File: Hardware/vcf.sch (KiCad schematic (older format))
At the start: 67 parts, among them U1 TL074, U2 TL074, U3 TL074

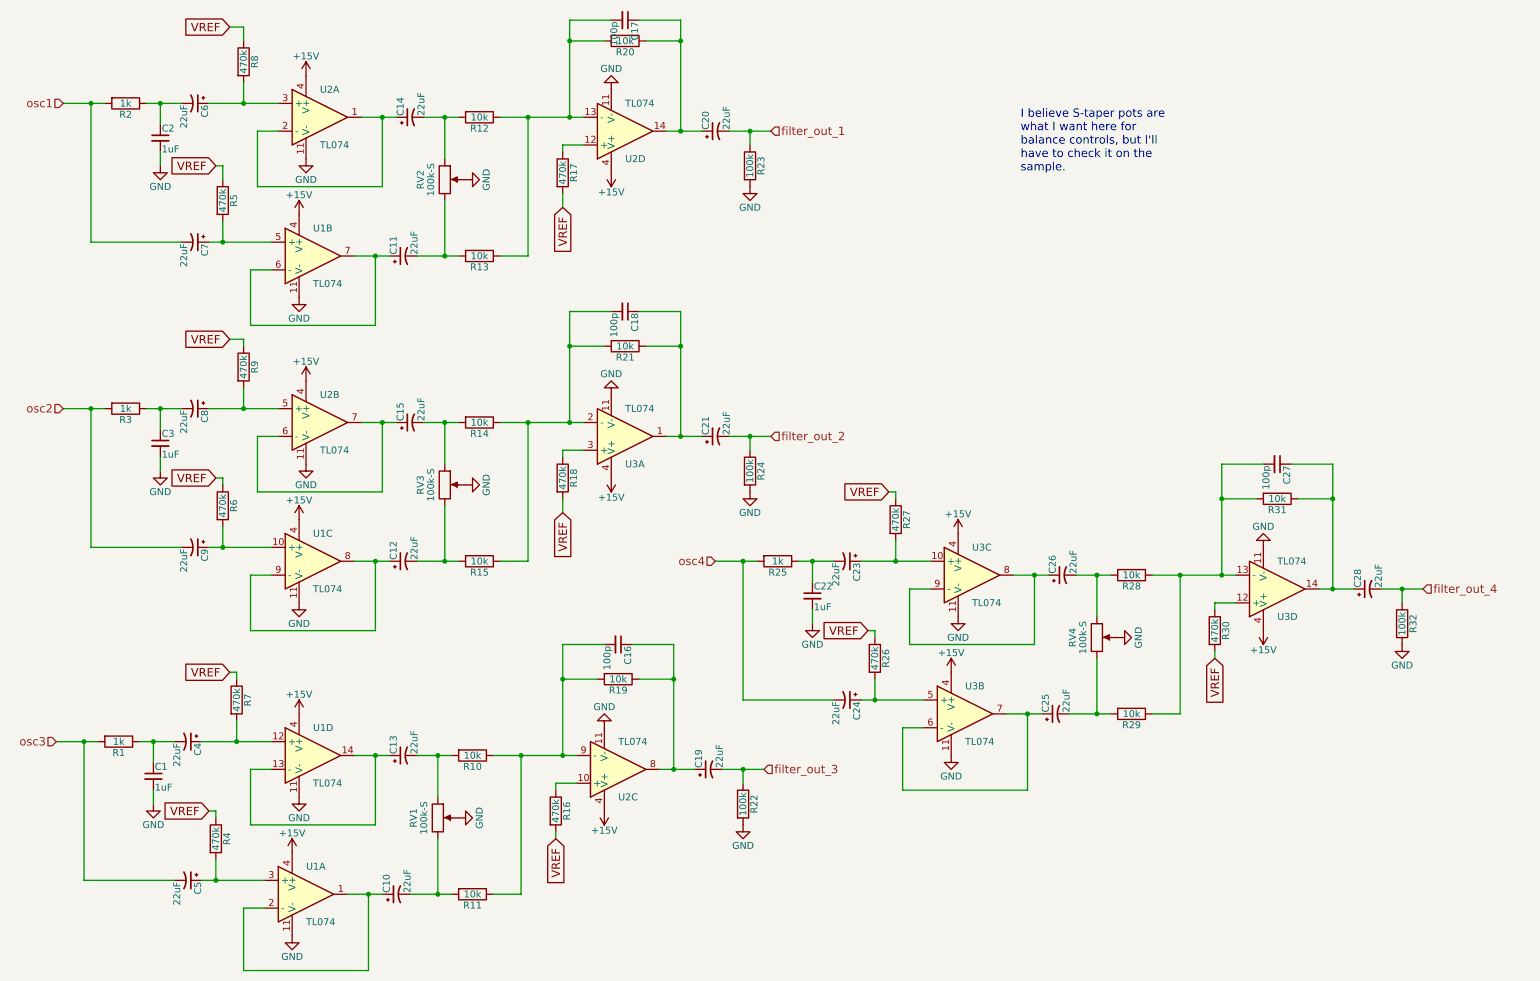
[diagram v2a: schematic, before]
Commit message: fix annotation and footprints for multi-part op amps.
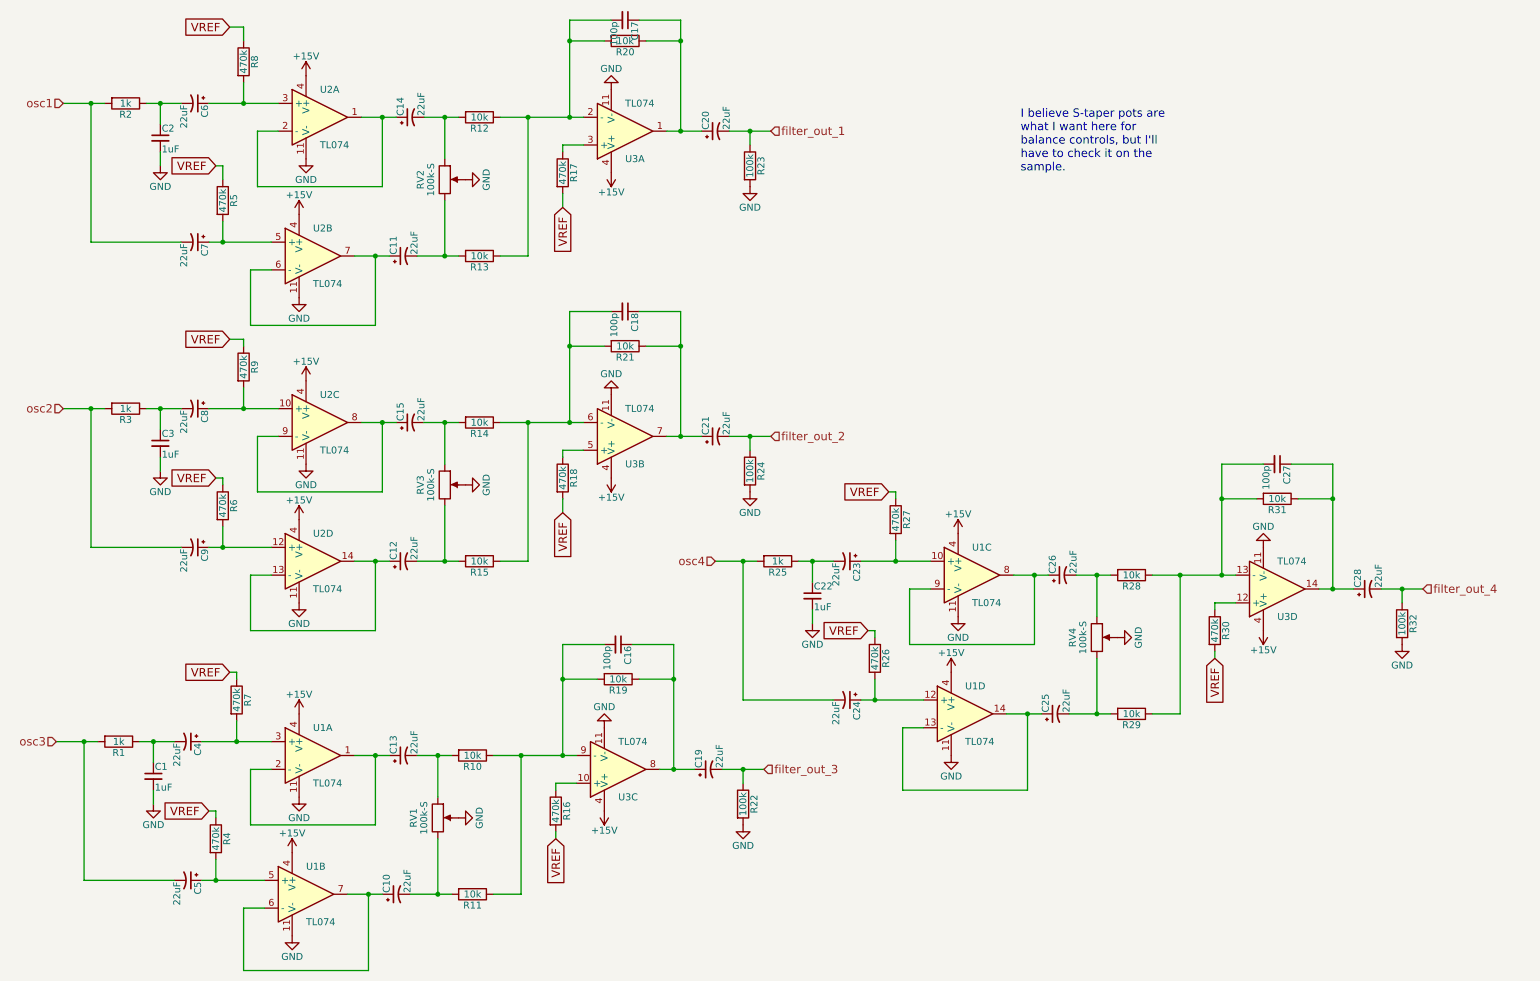
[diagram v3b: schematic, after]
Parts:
- renumbered U3 to U1, U1 to U2, U2 to U3
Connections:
- net at C17.2, R12.1, R13.1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: now also U3.2 (-); no longer U3.13 (-)
- net at R17.1: now also U3.3 (+); no longer U3.12 (+)
- net at C17.1, C20.1, R20.1: now also U3.1; no longer U3.14
- net at C8.1, R9.2: now also U2.10 (+); no longer U2.5 (+)
- net at C9.1, R6.2: now also U2.12 (+); no longer U2.10 (+)
- net at C18.2, R14.1, R15.1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: now also U3.6 (-); no longer U3.2 (-)
- net at C18.1, C21.1, R21.1: now also U3.7; no longer U3.1
- net at R18.1: now also U3.5 (+); no longer U3.3 (+)
- net at C4.1, R7.2: now also U1.3 (+); no longer U1.12 (+)
- net at C5.1, R4.2: now also U1.5 (+); no longer U1.3 (+)
- net at C24.1, R26.2: now also U1.12 (+); no longer U1.5 (+)
- new net: C15.1, U2.8, U2.9 (-)
- new net: C12.1, U2.13 (-), U2.14
- new net: C13.1, U1.1, U1.2 (-)
- new net: C10.1, U1.6 (-), U1.7
- new net: C25.1, U1.13 (-), U1.14
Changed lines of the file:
@@
 $EndComp
 $Comp
-L TL074 U1
+L TL074 U2
 U 2 1 5C37EB17
 P 2600 2200
-F 0 "U1" H 2600 2400 50  0000 L CNN
+F 0 "U2" H 2600 2400 50  0000 L CNN
 F 1 "TL074" H 2600 2000 50  0000 L CNN
 F 2 "digikey-footprints:SOIC-14_W3.9mm" H 2550 2300 50  0001 C CNN
@@
 $EndComp
 $Comp
-L TL074 U2
-U 4 1 5C37F61B
+L TL074 U3
+U 1 1 5C37F61B
 P 4850 1300
-F 0 "U2" H 4850 1500 50  0000 L CNN
+F 0 "U3" H 4850 1500 50  0000 L CNN
 F 1 "TL074" H 4850 1100 50  0000 L CNN
 F 2 "digikey-footprints:SOIC-14_W3.9mm" H 4800 1400 50  0001 C CNN
 F 3 "" H 4900 1500 50  0001 C CNN
-	4    4850 1300
+	1    4850 1300
 	1    0    0    1
 $EndComp
@@
 $Comp
 L TL074 U2
-U 2 1 5C389FC9
+U 3 1 5C389FC9
 P 2650 3400
 F 0 "U2" H 2650 3600 50  0000 L CNN
@@
 F 2 "digikey-footprints:SOIC-14_W3.9mm" H 2600 3500 50  0001 C CNN
 F 3 "" H 2700 3600 50  0001 C CNN
-	2    2650 3400
+	3    2650 3400
 	1    0    0    -1
 $EndComp
@@
 $EndComp
 $Comp
-L TL074 U1
-U 3 1 5C389FF8
+L TL074 U2
+U 4 1 5C389FF8
 P 2600 4400
-F 0 "U1" H 2600 4600 50  0000 L CNN
+F 0 "U2" H 2600 4600 50  0000 L CNN
 F 1 "TL074" H 2600 4200 50  0000 L CNN
 F 2 "digikey-footprints:SOIC-14_W3.9mm" H 2550 4500 50  0001 C CNN
 F 3 "" H 2650 4600 50  0001 C CNN
-	3    2600 4400
+	4    2600 4400
 	1    0    0    -1
 $EndComp
@@
 $Comp
 L TL074 U3
-U 1 1 5C38A035
+U 2 1 5C38A035
 P 4850 3500
 F 0 "U3" H 4850 3700 50  0000 L CNN
@@
 F 2 "digikey-footprints:SOIC-14_W3.9mm" H 4800 3600 50  0001 C CNN
 F 3 "" H 4900 3700 50  0001 C CNN
-	1    4850 3500
+	2    4850 3500
 	1    0    0    1
 $EndComp
@@
 $Comp
 L TL074 U1
-U 4 1 5C38A5BF
+U 1 1 5C38A5BF
 P 2600 5800
 F 0 "U1" H 2600 6000 50  0000 L CNN
@@
 F 2 "digikey-footprints:SOIC-14_W3.9mm" H 2550 5900 50  0001 C CNN
 F 3 "" H 2650 6000 50  0001 C CNN
-	4    2600 5800
+	1    2600 5800
 	1    0    0    -1
 $EndComp
@@
 $Comp
 L TL074 U1
-U 1 1 5C38A5EE
+U 2 1 5C38A5EE
 P 2550 6800
 F 0 "U1" H 2550 7000 50  0000 L CNN
@@
 F 2 "digikey-footprints:SOIC-14_W3.9mm" H 2500 6900 50  0001 C CNN
 F 3 "" H 2600 7000 50  0001 C CNN
-	1    2550 6800
+	2    2550 6800
 	1    0    0    -1
 $EndComp
@@
 $EndComp
 $Comp
-L TL074 U2
+L TL074 U3
 U 3 1 5C38A62B
 P 4800 5900
-F 0 "U2" H 4800 6100 50  0000 L CNN
+F 0 "U3" H 4800 6100 50  0000 L CNN
 F 1 "TL074" H 4800 5700 50  0000 L CNN
 F 2 "digikey-footprints:SOIC-14_W3.9mm" H 4750 6000 50  0001 C CNN
@@
 $EndComp
 $Comp
-L TL074 U3
+L TL074 U1
 U 3 1 5C38B2F3
 P 7350 4500
-F 0 "U3" H 7350 4700 50  0000 L CNN
+F 0 "U1" H 7350 4700 50  0000 L CNN
 F 1 "TL074" H 7350 4300 50  0000 L CNN
 F 2 "digikey-footprints:SOIC-14_W3.9mm" H 7300 4600 50  0001 C CNN
@@
 $EndComp
 $Comp
-L TL074 U3
-U 2 1 5C38B322
+L TL074 U1
+U 4 1 5C38B322
 P 7300 5500
-F 0 "U3" H 7300 5700 50  0000 L CNN
+F 0 "U1" H 7300 5700 50  0000 L CNN
 F 1 "TL074" H 7300 5300 50  0000 L CNN
 F 2 "digikey-footprints:SOIC-14_W3.9mm" H 7250 5600 50  0001 C CNN
 F 3 "" H 7350 5700 50  0001 C CNN
-	2    7300 5500
-	1    0    0    -1
-$EndComp
+	4    7300 5500
+	1    0    0    -1
+$EndComp

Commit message: complete initial PCB layout. CapSense buttons still not done, but everything else should be there. I had to increase to a 4-layer board to keep the dimensions 8"x4".
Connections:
- net +15V: now also U1.11 (V-); no longer U1.4 (V+)
- net GND: now also U1.4 (V+); no longer U1.11 (V-)
- net at C13.1, U1.1: now also U1.3 (+); no longer U1.2 (-)
- net at C4.1, R7.2: now also U1.2 (-); no longer U1.3 (+)
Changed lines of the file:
@@
 F 3 "" H 2650 6000 50  0001 C CNN
 	1    2600 5800
-	1    0    0    -1
+	1    0    0    1
 $EndComp
 $Comp

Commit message: some fixes from v1 boards. Power and GND are switched on one of the TL074s, fix an error in pot net connections. change firmware pinout to match boards. probably other minor things?
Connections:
- net +15V: now also U1.4 (V+); no longer U1.11 (V-)
- net GND: now also U1.11 (V-); no longer U1.4 (V+)
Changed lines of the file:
@@
 L GND #PWR014
 U 1 1 5C38A5E8
-P 2500 6100
-F 0 "#PWR014" H 2500 5850 50  0001 C CNN
-F 1 "GND" H 2500 5950 50  0000 C CNN
-F 2 "" H 2500 6100 50  0001 C CNN
-F 3 "" H 2500 6100 50  0001 C CNN
-	1    2500 6100
-	1    0    0    -1
+P 2500 5500
+F 0 "#PWR014" H 2500 5250 50  0001 C CNN
+F 1 "GND" H 2500 5350 50  0000 C CNN
+F 2 "" H 2500 5500 50  0001 C CNN
+F 3 "" H 2500 5500 50  0001 C CNN
+	1    2500 5500
+	-1   0    0    1
 $EndComp
 $Comp
@@
 L +15V #PWR029
 U 1 1 5C38E030
-P 2500 5500
-F 0 "#PWR029" H 2500 5350 50  0001 C CNN
-F 1 "+15V" H 2500 5640 50  0000 C CNN
-F 2 "" H 2500 5500 50  0001 C CNN
-F 3 "" H 2500 5500 50  0001 C CNN
-	1    2500 5500
-	1    0    0    -1
+P 2500 6100
+F 0 "#PWR029" H 2500 5950 50  0001 C CNN
+F 1 "+15V" H 2500 6240 50  0000 C CNN
+F 2 "" H 2500 6100 50  0001 C CNN
+F 3 "" H 2500 6100 50  0001 C CNN
+	1    2500 6100
+	-1   0    0    1
 $EndComp
 $Comp
@@
 	2200 1300 2350 1300
 Wire Wire Line
-	800  1100 1100 1100
+	800  1100 1000 1100
+Wire Wire Line
+	1000 1100 1100 1100
 Connection ~ 3100 1200
 Wire Wire Line
@@
 Connection ~ 2100 1100
 Wire Wire Line
-	1850 1100 2350 1100
-Wire Wire Line
-	2950 1200 3200 1200
+	1850 1100 2100 1100
+Wire Wire Line
+	2100 1100 2350 1100
+Wire Wire Line
+	2950 1200 3100 1200
+Wire Wire Line
+	3100 1200 3200 1200
 Wire Wire Line
 	3050 2200 3050 2700
@@
 	1000 2100 1650 2100
 Wire Wire Line
-	1850 2100 2300 2100
-Wire Wire Line
-	2900 2200 3150 2200
+	1850 2100 1950 2100
+Wire Wire Line
+	1950 2100 2300 2100
+Wire Wire Line
+	2900 2200 3050 2200
+Wire Wire Line
+	3050 2200 3150 2200
 Connection ~ 1000 1100
 Wire Wire Line
-	3950 1200 4550 1200
+	3950 1200 4150 1200
+Wire Wire Line
+	4150 1200 4450 1200
+Wire Wire Line
+	4450 1200 4550 1200
 Connection ~ 4150 1200
 Wire Wire Line
 	4700 650  4450 650
 Wire Wire Line
-	4450 500  4450 1200
+	4450 500  4450 650
+Wire Wire Line
+	4450 650  4450 1200
 Connection ~ 4450 1200
 Wire Wire Line
 	5000 650  5250 650
 Wire Wire Line
-	5250 500  5250 1300
-Wire Wire Line
-	5600 1300 5900 1300
+	5250 500  5250 650
+Wire Wire Line
+	5250 650  5250 1300
+Wire Wire Line
+	5600 1300 5750 1300
+Wire Wire Line
+	5750 1300 5900 1300
 Wire Wire Line
 	4400 1450 4400 1400
@@
 	1000 2100 1000 1100
 Wire Wire Line
-	1400 1100 1650 1100
+	1400 1100 1500 1100
+Wire Wire Line
+	1500 1100 1650 1100
 Connection ~ 1500 1100
 Wire Wire Line
-	5150 1300 5400 1300
+	5150 1300 5250 1300
+Wire Wire Line
+	5250 1300 5400 1300
 Connection ~ 5250 1300
 Wire Wire Line
-	3400 1200 3650 1200
+	3400 1200 3550 1200
+Wire Wire Line
+	3550 1200 3650 1200
 Wire Wire Line
 	3550 1500 3550 1200
 Connection ~ 3550 1200
 Wire Wire Line
-	3350 2200 3650 2200
+	3350 2200 3550 2200
+Wire Wire Line
+	3550 2200 3650 2200
 Wire Wire Line
 	3550 1800 3550 2200
@@
 	2200 3500 2350 3500
 Wire Wire Line
-	800  3300 1100 3300
+	800  3300 1000 3300
+Wire Wire Line
+	1000 3300 1100 3300
 Connection ~ 3100 3400
 Wire Wire Line
@@
 Connection ~ 2100 3300
 Wire Wire Line
-	1850 3300 2350 3300
-Wire Wire Line
-	2950 3400 3200 3400
+	1850 3300 2100 3300
+Wire Wire Line
+	2100 3300 2350 3300
+Wire Wire Line
+	2950 3400 3100 3400
+Wire Wire Line
+	3100 3400 3200 3400
 Wire Wire Line
 	3050 4400 3050 4900
@@
 	1000 4300 1650 4300
 Wire Wire Line
-	1850 4300 2300 4300
-Wire Wire Line
-	2900 4400 3150 4400
+	1850 4300 1950 4300
+Wire Wire Line
+	1950 4300 2300 4300
+Wire Wire Line
+	2900 4400 3050 4400
+Wire Wire Line
+	3050 4400 3150 4400
 Connection ~ 1000 3300
 Wire Wire Line
-	3950 3400 4550 3400
+	3950 3400 4150 3400
+Wire Wire Line
+	4150 3400 4450 3400
+Wire Wire Line
+	4450 3400 4550 3400
 Connection ~ 4150 3400
 Wire Wire Line
 	4700 2850 4450 2850
 Wire Wire Line
-	4450 2600 4450 3400
+	4450 2600 4450 2850
+Wire Wire Line
+	4450 2850 4450 3400
 Connection ~ 4450 3400
 Wire Wire Line
 	5000 2850 5250 2850
 Wire Wire Line
-	5250 2600 5250 3500
-Wire Wire Line
-	5600 3500 5900 3500
+	5250 2600 5250 2850
+Wire Wire Line
+	5250 2850 5250 3500
+Wire Wire Line
+	5600 3500 5750 3500
+Wire Wire Line
+	5750 3500 5900 3500
 Wire Wire Line
 	4400 3650 4400 3600
@@
 	1000 4300 1000 3300
 Wire Wire Line
-	1400 3300 1650 3300
+	1400 3300 1500 3300
+Wire Wire Line
+	1500 3300 1650 3300
 Connection ~ 1500 3300
 Wire Wire Line
-	5150 3500 5400 3500
+	5150 3500 5250 3500
+Wire Wire Line
+	5250 3500 5400 3500
 Connection ~ 5250 3500
 Wire Wire Line
-	3400 3400 3650 3400
+	3400 3400 3550 3400
+Wire Wire Line
+	3550 3400 3650 3400
 Wire Wire Line
 	3550 3700 3550 3400
 Connection ~ 3550 3400
 Wire Wire Line
-	3350 4400 3650 4400
+	3350 4400 3550 4400
+Wire Wire Line
+	3550 4400 3650 4400
 Wire Wire Line
 	3550 4000 3550 4400
@@
 	2150 5900 2300 5900
 Wire Wire Line
-	750  5700 1050 5700
+	750  5700 950  5700
+Wire Wire Line
+	950  5700 1050 5700
 Connection ~ 3050 5800
 Wire Wire Line
@@
 Connection ~ 2050 5700
 Wire Wire Line
-	1800 5700 2300 5700
-Wire Wire Line
-	2900 5800 3150 5800
+	1800 5700 2050 5700
+Wire Wire Line
+	2050 5700 2300 5700
+Wire Wire Line
+	2900 5800 3050 5800
+Wire Wire Line
+	3050 5800 3150 5800
 Wire Wire Line
 	3000 6800 3000 7350
@@
 	950  6700 1600 6700
 Wire Wire Line
-	1800 6700 2250 6700
-Wire Wire Line
-	2850 6800 3100 6800
+	1800 6700 1900 6700
+Wire Wire Line
+	1900 6700 2250 6700
+Wire Wire Line
+	2850 6800 3000 6800
+Wire Wire Line
+	3000 6800 3100 6800
 Connection ~ 950  5700
 Wire Wire Line
-	3900 5800 4500 5800
+	3900 5800 4100 5800
+Wire Wire Line
+	4100 5800 4400 5800
+Wire Wire Line
+	4400 5800 4500 5800
 Connection ~ 4100 5800
 Wire Wire Line
 	4650 5250 4400 5250
 Wire Wire Line
-	4400 5000 4400 5800
+	4400 5000 4400 5250
+Wire Wire Line
+	4400 5250 4400 5800
 Connection ~ 4400 5800
 Wire Wire Line
 	4950 5250 5200 5250
 Wire Wire Line
-	5200 5000 5200 5900
-Wire Wire Line
-	5550 5900 5850 5900
+	5200 5000 5200 5250
+Wire Wire Line
+	5200 5250 5200 5900
+Wire Wire Line
+	5550 5900 5700 5900
+Wire Wire Line
+	5700 5900 5850 5900
 Wire Wire Line
 	4350 6050 4350 6000
@@
 	950  6700 950  5700
 Wire Wire Line
-	1350 5700 1600 5700
+	1350 5700 1450 5700
+Wire Wire Line
+	1450 5700 1600 5700
 Connection ~ 1450 5700
 Wire Wire Line
-	5100 5900 5350 5900
+	5100 5900 5200 5900
+Wire Wire Line
+	5200 5900 5350 5900
 Connection ~ 5200 5900
 Wire Wire Line
-	3350 5800 3600 5800
+	3350 5800 3500 5800
+Wire Wire Line
+	3500 5800 3600 5800
 Wire Wire Line
 	3500 6100 3500 5800
 Connection ~ 3500 5800
 Wire Wire Line
-	3300 6800 3600 6800
+	3300 6800 3500 6800
+Wire Wire Line
+	3500 6800 3600 6800
 Wire Wire Line
 	3500 6400 3500 6800
@@
 	6900 4600 7050 4600
 Wire Wire Line
-	5500 4400 5800 4400
+	5500 4400 5700 4400
+Wire Wire Line
+	5700 4400 5800 4400
 Connection ~ 7800 4500
 Wire Wire Line
@@
 Connection ~ 6800 4400
 Wire Wire Line
-	6550 4400 7050 4400
-Wire Wire Line
-	7650 4500 7900 4500
+	6550 4400 6800 4400
+Wire Wire Line
+	6800 4400 7050 4400
+Wire Wire Line
+	7650 4500 7800 4500
+Wire Wire Line
+	7800 4500 7900 4500
 Wire Wire Line
 	7750 5500 7750 6050
@@
 	5700 5400 6350 5400
 Wire Wire Line
-	6550 5400 7000 5400
-Wire Wire Line
-	7600 5500 7850 5500
+	6550 5400 6650 5400
+Wire Wire Line
+	6650 5400 7000 5400
+Wire Wire Line
+	7600 5500 7750 5500
+Wire Wire Line
+	7750 5500 7850 5500
 Connection ~ 5700 4400
 Wire Wire Line
-	8650 4500 9250 4500
+	8650 4500 8850 4500
+Wire Wire Line
+	8850 4500 9150 4500
+Wire Wire Line
+	9150 4500 9250 4500
 Connection ~ 8850 4500
 Wire Wire Line
 	9400 3950 9150 3950
 Wire Wire Line
-	9150 3700 9150 4500
+	9150 3700 9150 3950
+Wire Wire Line
+	9150 3950 9150 4500
 Connection ~ 9150 4500
 Wire Wire Line
 	9700 3950 9950 3950
 Wire Wire Line
-	9950 3700 9950 4600
-Wire Wire Line
-	10300 4600 10600 4600
+	9950 3700 9950 3950
+Wire Wire Line
+	9950 3950 9950 4600
+Wire Wire Line
+	10300 4600 10450 4600
+Wire Wire Line
+	10450 4600 10600 4600
 Wire Wire Line
 	9100 4750 9100 4700
@@
 	5700 5400 5700 4400
 Wire Wire Line
-	6100 4400 6350 4400
+	6100 4400 6200 4400
+Wire Wire Line
+	6200 4400 6350 4400
 Connection ~ 6200 4400
 Wire Wire Line
-	9850 4600 10100 4600
+	9850 4600 9950 4600
+Wire Wire Line
+	9950 4600 10100 4600
 Connection ~ 9950 4600
 Wire Wire Line
-	8100 4500 8350 4500
+	8100 4500 8250 4500
+Wire Wire Line
+	8250 4500 8350 4500
 Wire Wire Line
 	8250 4800 8250 4500
 Connection ~ 8250 4500
 Wire Wire Line
-	8050 5500 8350 5500
+	8050 5500 8250 5500
+Wire Wire Line
+	8250 5500 8350 5500
 Wire Wire Line
 	8250 5100 8250 5500
